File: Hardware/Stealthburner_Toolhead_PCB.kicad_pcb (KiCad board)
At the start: 4 copper layers, 47 x 40 mm, 144 parts, among them J1 Conn_01x02, J10 Conn_01x05, J11 Conn_01x04, J12 Conn_01x04, J2 Conn_01x03, J3 TestPoint, J4 Conn_01x02, J5 Conn_01x03, J6 Conn_01x02, J7 Conn_01x05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

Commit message: bugs fix
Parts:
- removed kibuzzard-62BD8832: G***, kibuzzard-62BD8832
- added kibuzzard-62F0BBF4: G***, kibuzzard-62F0BBF4, B.Cu at (119.2, 98.2)
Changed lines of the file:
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@@
-      ) (layer "B.SilkS") (width 0) (fill solid))
-  )
-  (footprint "kibuzzard-62BD8832" (layer "B.Cu")
-    (at 119.1768 98.2472 180)
-    (descr "Generated with KiBuzzard")
-    (tags "kb_params=eyJBbGlnbm1lbnRDaG9pY2UiOiAiQ2VudGVyIiwgIkNhcExlZnRDaG9pY2UiOiAiWyIsICJDYXBSaWdodENob2ljZSI6ICJdIiwgIkZvbnRDb21ib0JveCI6ICJtcGx1cy0xbW4tbWVkaXVtIiwgIkhlaWdodEN0cmwiOiAiMC44IiwgIkxheWVyQ29tYm9Cb3giOiAiRi5TaWxrUyIsICJNdWx0aUxpbmVUZXh0IjogIjQxIiwgIlBhZGRpbmdCb3R0b21DdHJsIjogIjMiLCAiUGFkZGluZ0xlZnRDdHJsIjogIjMiLCAiUGFkZGluZ1JpZ2h0Q3RybCI6ICIzIiwgIlBhZGRpbmdUb3BDdHJsIjogIjMiLCAiV2lkdGhDdHJsIjogIjEuMyJ9")
-    (attr board_only exclude_from_pos_files exclude_from_bom)
-    (fp_text reference "kibuzzard-62BD8832" (at 0 3.6703) (layer "B.SilkS") hide
-      (effects (font (size 0.7 0.7) (thickness 0.12)) (justify mirror))
-    )
-    (fp_text value "G***" (at 0 -3.6703) (layer "B.SilkS") hide
-      (effects (font (size 0 0) (thickness 0.15)) (justify mirror))
-    )
-    (fp_poly (pts
-        (xy -0.526415 0.6223)
-        (xy -0.685165 0.6223)
-        (xy -0.685165 -0.6223)
-        (xy -0.526415 -0.6223)
-        (xy -0.071755 -0.6223)
-        (xy -0.071755 -0.46355)
-        (xy -0.211455 -0.46355)
-        (xy -0.211455 -0.25781)
-        (xy -0.526415 -0.25781)
-        (xy -0.526415 -0.14859)
-        (xy -0.225425 0.46355)
-        (xy -0.071755 0.46355)
-        (xy -0.071755 -0.14859)
-        (xy 0.032385 -0.14859)
-        (xy 0.032385 -0.25781)
-        (xy -0.071755 -0.25781)
-        (xy -0.071755 -0.46355)
-        (xy -0.071755 -0.6223)
-        (xy 0.384175 -0.6223)
-        (xy 0.384175 -0.46355)
-        (xy 0.384175 0.3302)
-        (xy 0.381635 0.33147)
-        (xy 0.163195 0.20955)
-        (xy 0.163195 0.33401)
-        (xy 0.385445 0.46355)
-        (xy 0.526415 0.46355)
-        (xy 0.526415 -0.46355)
-        (xy 0.384175 -0.46355)
-        (xy 0.384175 -0.6223)
-        (xy 0.526415 -0.6223)
-        (xy 0.685165 -0.6223)
-        (xy 0.685165 0.6223)
-        (xy 0.526415 0.6223)
-        (xy -0.526415 0.6223)
-      ) (layer "B.SilkS") (width 0) (fill solid))
-    (fp_poly (pts
-        (xy -0.211455 -0.14859)
-        (xy -0.211455 0.2667)
-        (xy -0.213995 0.2667)
-        (xy -0.414655 -0.14478)
-        (xy -0.414655 -0.14859)
-        (xy -0.211455 -0.14859)
       ) (layer "B.SilkS") (width 0) (fill solid))
   )
@@
     )
   )
+  (footprint "kibuzzard-62F0BBF4" (layer "B.Cu")
+    (at 119.1768 98.2472 180)
+    (descr "Generated with KiBuzzard")
+    (tags "kb_params=eyJBbGlnbm1lbnRDaG9pY2UiOiAiQ2VudGVyIiwgIkNhcExlZnRDaG9pY2UiOiAiWyIsICJDYXBSaWdodENob2ljZSI6ICJdIiwgIkZvbnRDb21ib0JveCI6ICJtcGx1cy0xbW4tbWVkaXVtIiwgIkhlaWdodEN0cmwiOiAiMC44IiwgIkxheWVyQ29tYm9Cb3giOiAiRi5TaWxrUyIsICJNdWx0aUxpbmVUZXh0IjogIjI5IiwgIlBhZGRpbmdCb3R0b21DdHJsIjogIjMiLCAiUGFkZGluZ0xlZnRDdHJsIjogIjMiLCAiUGFkZGluZ1JpZ2h0Q3RybCI6ICIzIiwgIlBhZGRpbmdUb3BDdHJsIjogIjMiLCAiV2lkdGhDdHJsIjogIjEuMyJ9")
+    (attr board_only exclude_from_pos_files exclude_from_bom)
+    (fp_text reference "kibuzzard-62F0BBF4" (at 0 3.683) (layer "B.SilkS") hide
+      (effects (font (size 0 0)) (justify mirror))
+    )
+    (fp_text value "G***" (at 0 -3.683) (layer "B.SilkS") hide
+      (effects (font (size 0 0)) (justify mirror))
+    )
+    (fp_poly (pts
+        (xy 0.30226 0.36703)
+        (xy 0.251143 0.356076)
+        (xy 0.21717 0.323215)
+        (xy 0.19812 0.260826)
+        (xy 0.19177 0.16129)
+        (xy 0.197961 0.060642)
+        (xy 0.216535 -0.00254)
+        (xy 0.249079 -0.035878)
+        (xy 0.29718 -0.04699)
+        (xy 0.347186 -0.03429)
+        (xy 0.382905 0.00381)
+        (xy 0.404336 0.06731)
+        (xy 0.41148 0.15621)
+        (xy 0.404813 0.255587)
+        (xy 0.38481 0.32004)
+        (xy 0.350838 0.355282)
+        (xy 0.30226 0.36703)
+      ) (layer "B.SilkS") (width 0) (fill solid))
+    (fp_poly (pts
+        (xy -0.55372 0.635)
+        (xy -0.71247 0.635)
+        (xy -0.71247 -0.635)
+        (xy -0.55372 -0.635)
+        (xy -0.09652 -0.635)
+        (xy -0.09652 -0.46355)
+        (xy -0.55372 -0.46355)
+        (xy -0.55372 -0.35306)
+        (xy -0.472181 -0.258277)
+        (xy -0.403186 -0.167692)
+        (xy -0.346736 -0.081306)
+        (xy -0.30283 0.000881)
+        (xy -0.271469 0.07887)
+        (xy -0.252652 0.152659)
+        (xy -0.24638 0.22225)
+        (xy -0.253206 0.28702)
+        (xy -0.273685 0.33147)
+        (xy -0.35687 0.36576)
+        (xy -0.41656 0.357434)
+        (xy -0.482177 0.332458)
+        (xy -0.55372 0.29083)
+        (xy -0.55372 0.41021)
+        (xy -0.483447 0.446899)
+        (xy -0.408093 0.468912)
+        (xy -0.32766 0.47625)
+        (xy -0.231299 0.460534)
+        (xy -0.160655 0.413385)
+        (xy -0.117316 0.335756)
+        (xy -0.10287 0.2286)
+        (xy -0.110843 0.148167)
+        (xy -0.134761 0.062653)
+        (xy -0.174625 -0.02794)
+        (xy -0.216019 -0.100489)
+        (xy -0.268446 -0.178435)
+        (xy -0.331907 -0.261779)
+        (xy -0.4064 -0.35052)
+        (xy -0.4064 -0.35306)
+        (xy -0.09652 -0.35306)
+        (xy -0.09652 -0.46355)
+        (xy -0.09652 -0.635)
+        (xy 0.26797 -0.635)
+        (xy 0.26797 -0.47625)
+        (xy 0.187007 -0.4699)
+        (xy 0.10922 -0.45085)
+        (xy 0.10922 -0.3302)
+        (xy 0.17907 -0.35687)
+        (xy 0.25146 -0.36576)
+        (xy 0.321469 -0.352108)
+        (xy 0.368935 -0.31115)
+        (xy 0.389749 -0.263596)
+        (xy 0.403931 -0.193746)
+        (xy 0.41148 -0.1016)
+        (xy 0.40767 -0.1016)
+        (xy 0.342582 -0.142558)
+        (xy 0.27178 -0.15621)
+        (xy 0.176054 -0.137636)
+        (xy 0.107315 -0.081915)
+        (xy 0.076623 -0.021872)
+        (xy 0.058208 0.059196)
+        (xy 0.05207 0.16129)
+        (xy 0.058914 0.260703)
+        (xy 0.079446 0.340501)
+        (xy 0.113665 0.400685)
+        (xy 0.161996 0.442666)
+        (xy 0.224861 0.467854)
+        (xy 0.30226 0.47625)
+        (xy 0.38608 0.466513)
+        (xy 0.451273 0.437303)
+        (xy 0.49784 0.38862)
+        (xy 0.522288 0.335042)
+        (xy 0.53975 0.261938)
+        (xy 0.550228 0.169307)
+        (xy 0.55372 0.05715)
+        (xy 0.551736 -0.040203)
+        (xy 0.545783 -0.126524)
+        (xy 0.535861 -0.201811)
+        (xy 0.52197 -0.266065)
+        (xy 0.483076 -0.36576)
+        (xy 0.429895 -0.429895)
+        (xy 0.359251 -0.464661)
+        (xy 0.26797 -0.47625)
+        (xy 0.26797 -0.635)
+        (xy 0.55372 -0.635)
+        (xy 0.71247 -0.635)
+        (xy 0.71247 0.635)
+        (xy 0.55372 0.635)
+        (xy -0.55372 0.635)
+      ) (layer "B.SilkS") (width 0) (fill solid))
+  )
   (footprint "Package_TO_SOT_SMD:SOT-23" (layer "B.Cu")

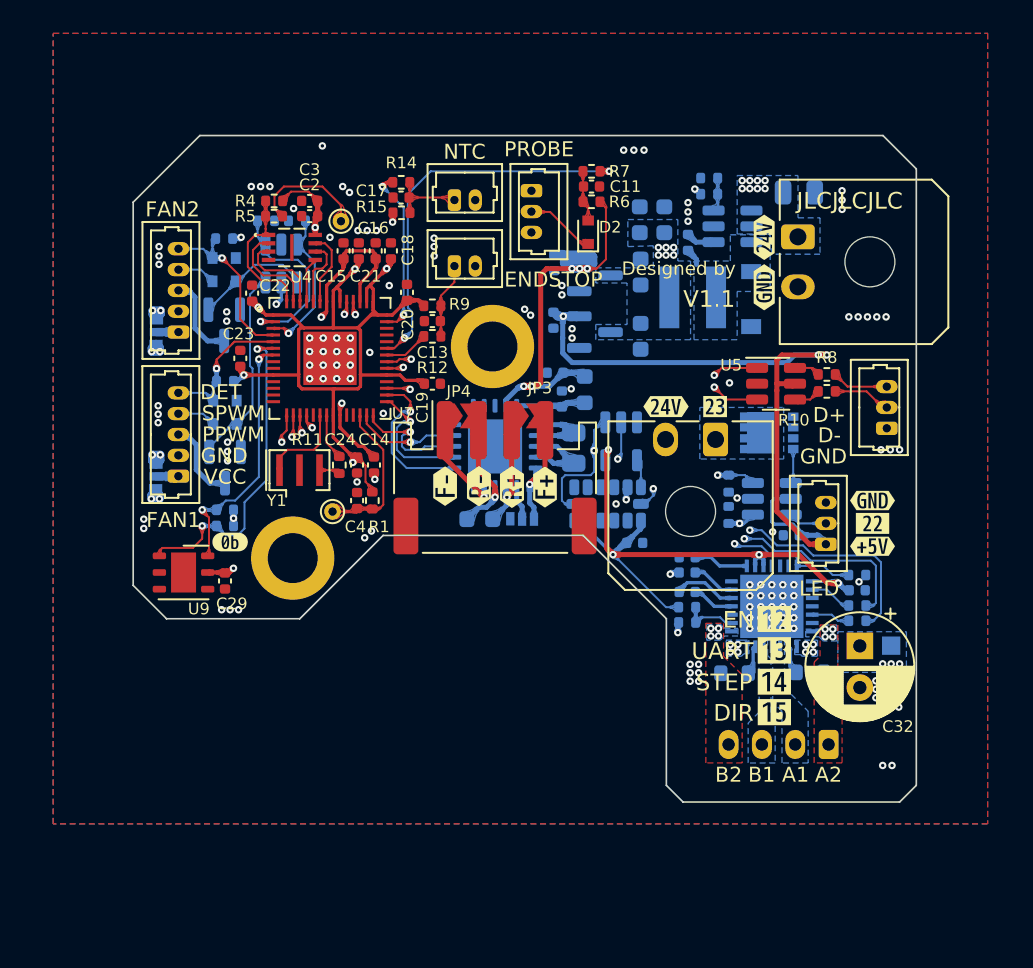
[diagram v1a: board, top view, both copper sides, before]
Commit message: V1.2 Release
*Changelog*

* 略微修改PCB尺寸与原件布局，防止板子与打印件干涉
* 删除了温度传感器周围的铺铜
* 修复一些小bug
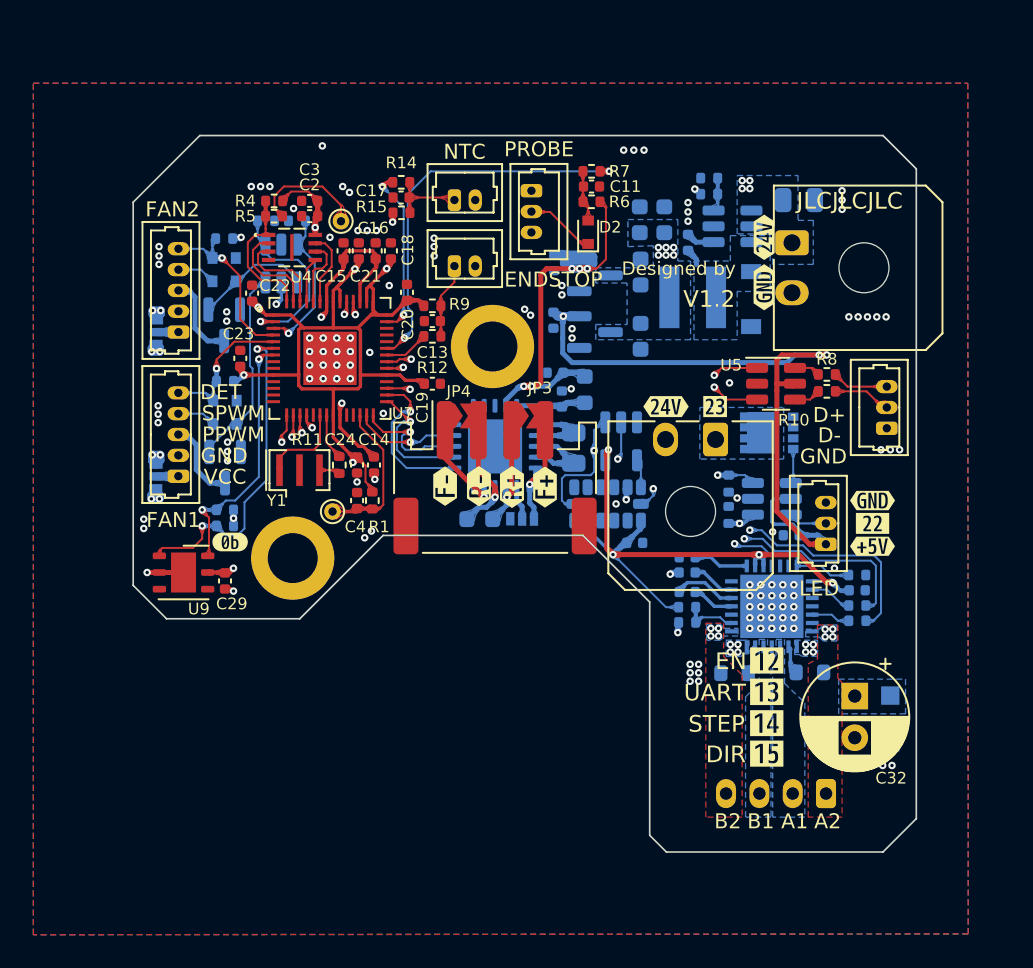
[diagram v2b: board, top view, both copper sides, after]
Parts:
- removed kibuzzard-62BD8821: G***, kibuzzard-62BD8821
- added kibuzzard-6309F118: G***, kibuzzard-6309F118, B.Cu at (119.2, 102.2)
- moved C32 3.03 mm to (143.3, 129.6)
- moved D7 3.00 mm to (145.4, 131.0)
- moved J12 2.95 mm to (141.6, 135.5)
- moved kibuzzard-62BB1FE8 2.53 mm to (138.0, 131.3)
- moved kibuzzard-62BB1FEC 2.53 mm to (138.0, 133.1)
- moved kibuzzard-62BB1FE0 2.53 mm to (138.0, 127.5)
- moved kibuzzard-62BB1FE5 2.53 mm to (138.0, 129.4)
- moved J1 0.50 mm to (139.5, 102.4)
- moved C1 0.46 mm to (140.0, 99.9)
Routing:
- net GND: track 0.00 -> 2.75 mm, vias 121 -> 114
- net +24V: track 70.6 -> 68.7 mm, vias 24 -> 17
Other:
- board size 47 x 40 mm -> 47 x 43 mm
- board text added: "V1.2"
- board text removed: "V1.1"

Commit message: V2.1 Replace Molex PicoBlade Connector with PH2.0 Connector Replace USB connector with Micro USB port Modified PCB size
将1.25mm连接器替换为2.0mm
使用MicroUSB母座作为USB连接器
修改PCB尺寸
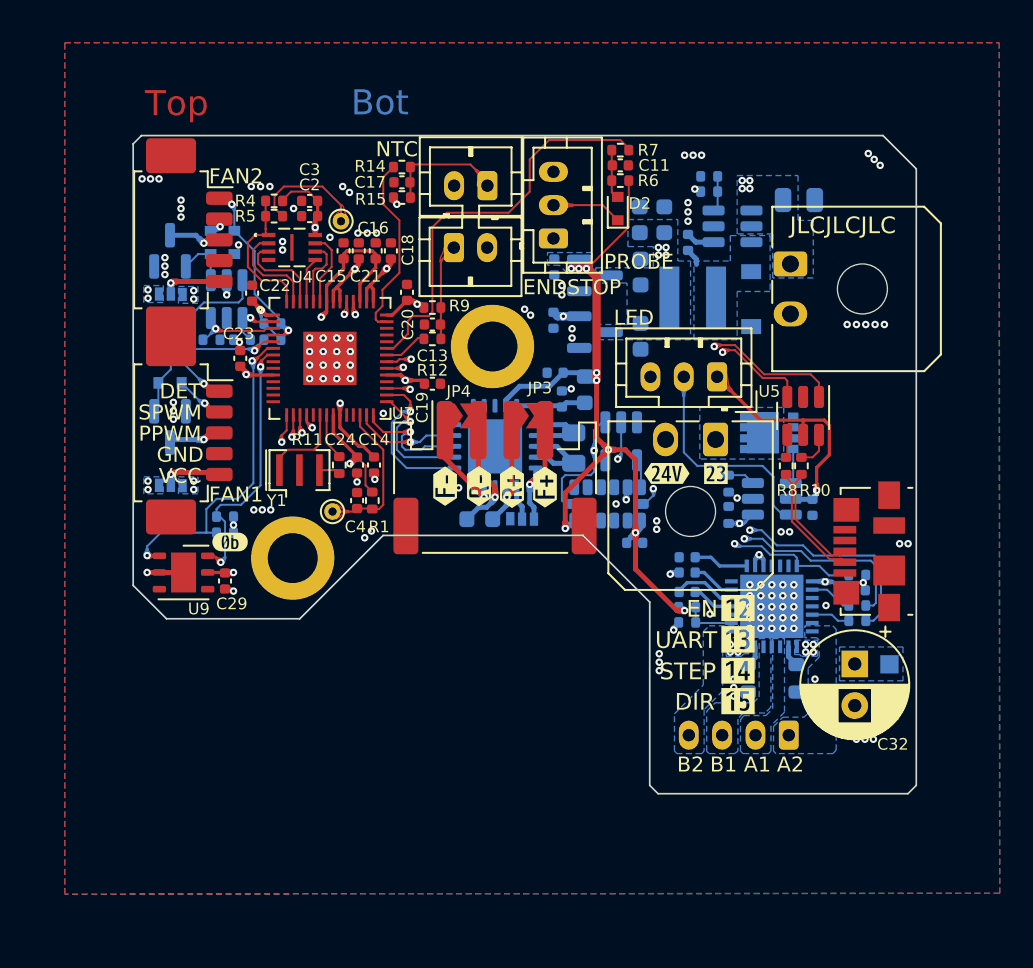
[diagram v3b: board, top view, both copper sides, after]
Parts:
- removed kibuzzard-62BB2432: G***, kibuzzard-62BB2432
- removed kibuzzard-62BB2448: G***, kibuzzard-62BB2448
- removed kibuzzard-62BB2459: G***, kibuzzard-62BB2459
- added G***: LOGO, LOGO, F.Cu at (144.5, 113.8)
- added kibuzzard-63148E7F: G***, kibuzzard-63148E7F, B.Cu at (133.0, 112.0)
- added kibuzzard-63148E89: G***, kibuzzard-63148E89, B.Cu at (135.1, 112.0)
- added kibuzzard-63148E96: G***, kibuzzard-63148E96, B.Cu at (131.0, 112.0)
- G***, kibuzzard-62BB2226, kibuzzard-62BB2232: moved to B.Cu
- J10, J7: footprint 1_Library:Molex_PicoBlade_53047-0510_1x05_P1.25mm_Vertical -> Connector_Molex:Molex_PicoBlade_53261-0571_1x05-1MP_P1.25mm_Horizontal
- J2, J8: footprint 1_Library:Molex_PicoBlade_53047-0310_1x03_P1.25mm_Vertical -> Connector_JST:JST_PH_B3B-PH-K_1x03_P2.00mm_Vertical
- J4, J6: footprint 1_Library:Molex_PicoBlade_53047-0210_1x02_P1.25mm_Vertical -> Connector_JST:JST_PH_B2B-PH-K_1x02_P2.00mm_Vertical
- J5: value Conn_01x03 -> USB_B_Micro; footprint 1_Library:Molex_PicoBlade_53047-0310_1x03_P1.25mm_Vertical -> Connector_USB:USB_Micro-B_Molex_47346-0001
- U12: value TMC2209-LA-T -> QFN28_5X5_3X8_EPAD_TRI
- U4: value W25Q16JVUXIQ -> W25Q16JVUXIQ_WIN
- moved G*** 13.7 mm to (143.0, 115.2), turned to -90 degrees
- moved J8 12.0 mm to (135.0, 110.5), turned to 180 degrees
- moved R18 8.79 mm to (104.7, 108.3), turned to 0 degrees
- moved J5 7.46 mm to (144.2, 121.0)
- moved R13 7.28 mm to (106.5, 108.3), turned to 180 degrees
- moved R8 6.00 mm to (139.2, 115.8), turned to -90 degrees
- moved R20 5.87 mm to (108.4, 107.3), turned to 0 degrees
- moved J10 5.54 mm to (102.8, 102.3), turned to -90 degrees
- moved Q2 5.53 mm to (102.2, 102.9), turned to 90 degrees
- moved kibuzzard-62BB2232 4.93 mm to (121.4, 97.2)
- moved R10 4.72 mm to (140.1, 115.8), turned to 90 degrees
- moved J12 4.16 mm to (139.3, 132.0)
- moved D3 4.12 mm to (102.2, 110.8), turned to 0 degrees
- moved D4 4.10 mm to (102.2, 109.5), turned to 0 degrees
- moved Q1 4.10 mm to (102.2, 113.5)
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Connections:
- J10 pad 1: Net-(J10-Pad1) -> /FAN2_DET
- J10 pad 2: GND -> Net-(D5-Pad2)
- J10 pad 4: Net-(D5-Pad2) -> GND
- J10 pad 5: /FAN2_DET -> Net-(J10-Pad5)
- J5 pad 1: GND -> unconnected-(J5-Pad1)
- J7 pad 1: Net-(J7-Pad1) -> /FAN1_DET
- J7 pad 2: GND -> Net-(D3-Pad2)
- J7 pad 4: Net-(D3-Pad2) -> GND
- J7 pad 5: /FAN1_DET -> Net-(J7-Pad5)
- JP1 pad 2: Net-(J7-Pad1) -> Net-(J7-Pad5)
- JP2 pad 2: Net-(J10-Pad1) -> Net-(J10-Pad5)
- R10 pad 1: Net-(J5-Pad2) -> Net-(J5-Pad3)
- R8 pad 2: Net-(J5-Pad3) -> Net-(J5-Pad2)
- U5 pad 1: /D- -> /D+
- U5 pad 3: /D+ -> /D-
- U5 pad 4: Net-(R10-Pad2) -> Net-(R8-Pad1)
- U5 pad 6: Net-(R8-Pad1) -> Net-(R10-Pad2)
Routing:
- net Net-(J8-Pad2): track 2.32 -> 13.5 mm
- net +5V: track 63.5 -> 52.4 mm, vias 4 -> 3
- net +12V: track 67.8 -> 57.9 mm, vias 11 -> 9
- net /FAN1_PWM: track 11.2 -> 3.45 mm
- net +3V3: track 193.5 -> 187.2 mm, vias 19 -> 22
- net /D-: track 29.1 -> 34.9 mm
- net /D+: track 30.0 -> 35.0 mm
- net /FAN2_PWM: track 9.09 -> 5.37 mm
- net Net-(J5-Pad2): track 3.49 -> 7.16 mm
- net Net-(J7-Pad5): track 0.00 -> 3.67 mm, vias 0 -> 1
- net Net-(D5-Pad1): track 7.03 -> 3.37 mm
- net Net-(J10-Pad5): track 0.00 -> 3.61 mm, vias 0 -> 1
- net Net-(J5-Pad3): track 3.39 -> 6.81 mm
- net Net-(C17-Pad1): track 4.62 -> 7.19 mm
- net Net-(J10-Pad3): track 5.10 -> 3.24 mm, vias 0 -> 1
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- added copper zone on B.Cu, net +3V3
- removed copper zone on In1.Cu, net /D+
- removed copper zone on F.Cu, net /E-A2
- removed copper zone on F.Cu, net /E-B2
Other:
- board size 47 x 43 mm -> 47 x 39.5 mm
- board text added: "3"
- board text added: "Bot"
- board text added: "In1"
- board text added: "In2"
- board text added: "Top"
- board text added: "V2.1"
- board text removed: "D+"
- board text removed: "D-"
- board text removed: "Designed by"
- board text removed: "V1.2"
